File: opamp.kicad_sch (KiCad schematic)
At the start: 20 parts, among them J62 Conn_01x05, J63 Conn_01x02, J64 Conn_01x02, J65 Conn_01x02, J66 Conn_01x02, J67 Conn_01x05, Q10 SS8050, Q11 SS8050, Q12 SS8050, Q13 SS8050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

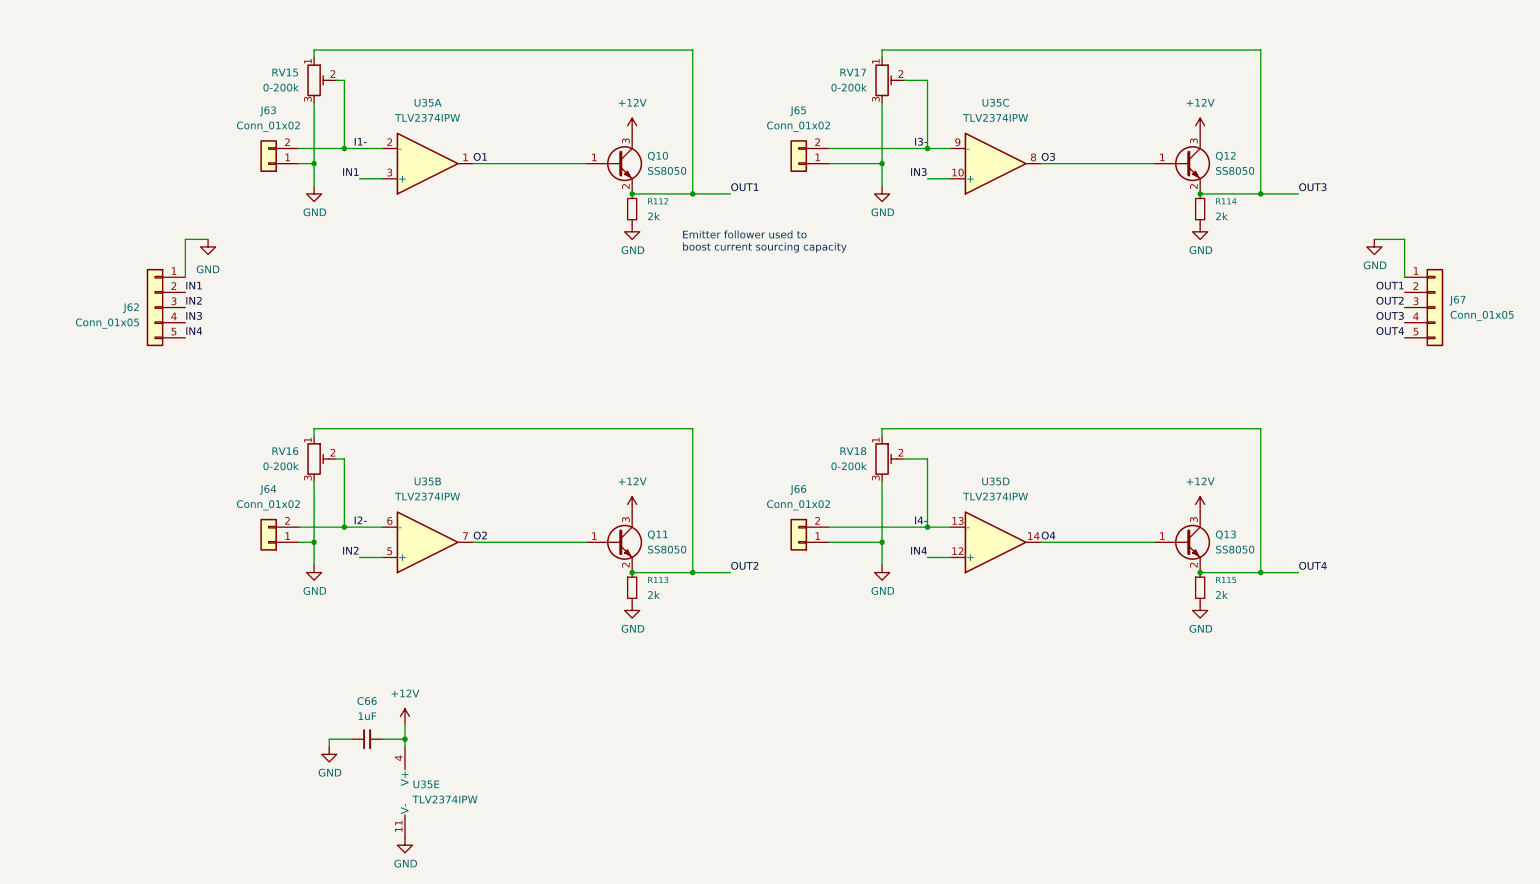
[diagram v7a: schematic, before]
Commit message: Adjust trimmer test pads
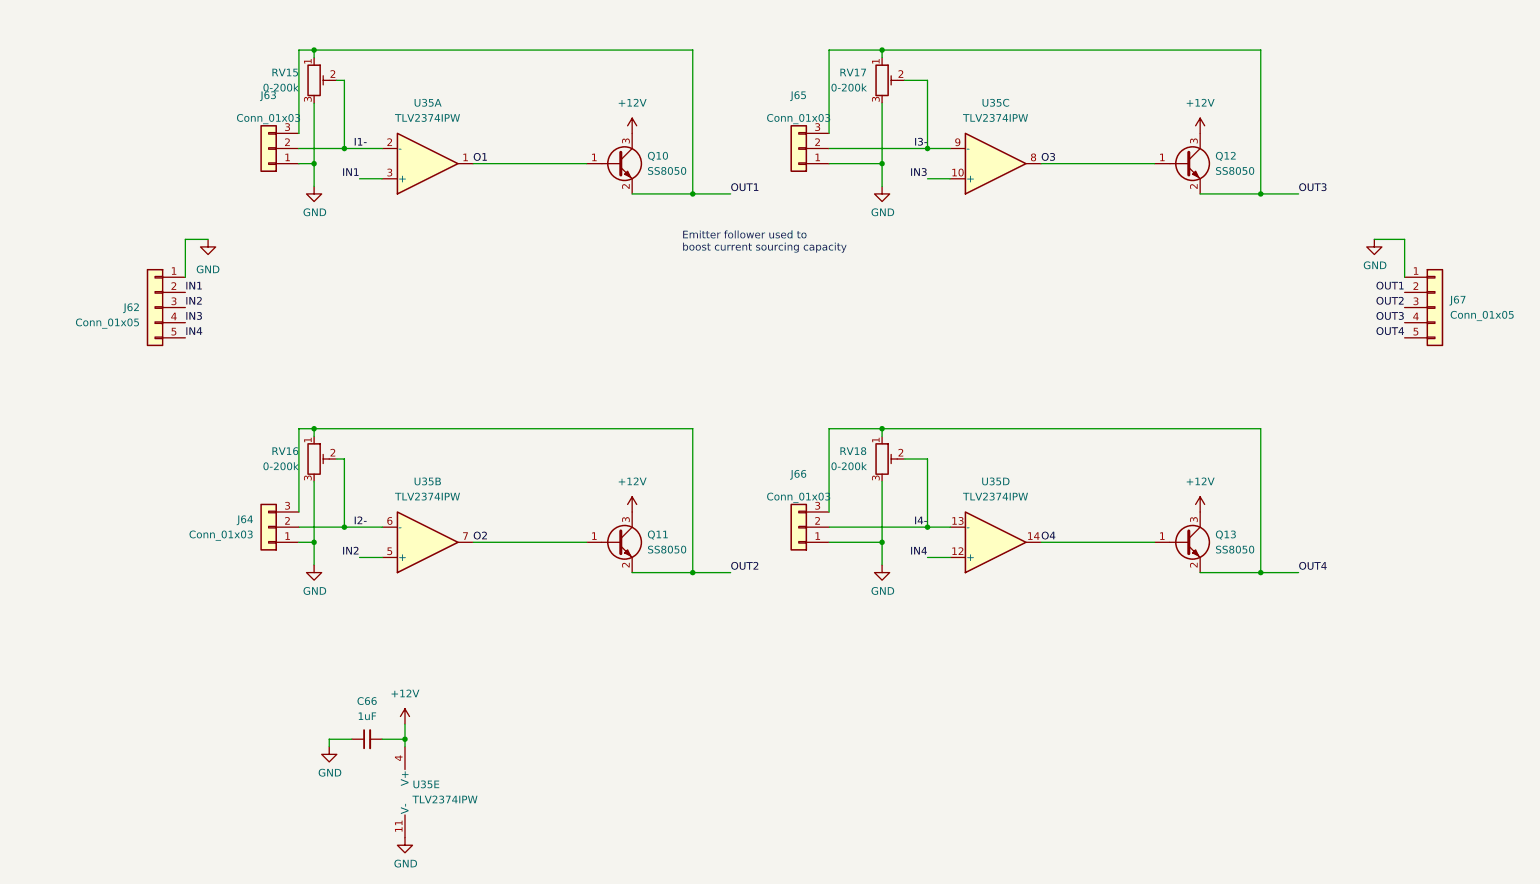
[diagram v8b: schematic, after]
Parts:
- removed R112, R113, R114, R115: 2k, Resistor_SMD:R_0603_1608Metric_Pad0.98x0.95mm_HandSolder, symbol Device:R_Small
- J63, J64, J65, J66: value Conn_01x02 -> Conn_01x03; footprint HL_Connector_Pad_2.00mm:Pad_1x02_P2.00_1.35x1.35_Rect-Oct -> HL_Connector_Pad_2.00mm:Pad_1x03_P2.00_1.35x1.35_Rect-2Oct; symbol Connector_Generic:Conn_01x02 -> Connector_Generic:Conn_01x03
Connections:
- net OUT1: now also J63.3 (Pin_3)
- net OUT2: now also J64.3 (Pin_3)
- net OUT3: now also J65.3 (Pin_3)
- net OUT4: now also J66.3 (Pin_3)
